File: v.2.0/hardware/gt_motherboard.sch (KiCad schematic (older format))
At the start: 68 parts, among them Q1 MMBT2222, Q2 IRLML6302, Q3 MMBT2222, SW1 SWITCH, U1 L6470

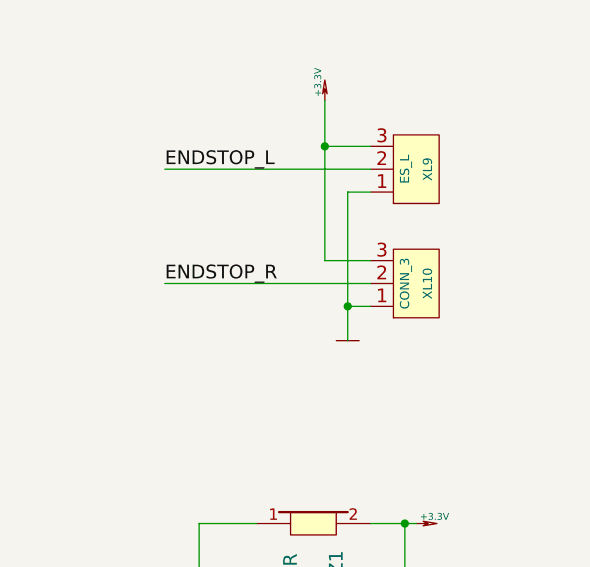
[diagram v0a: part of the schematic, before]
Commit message: + Assign all components.
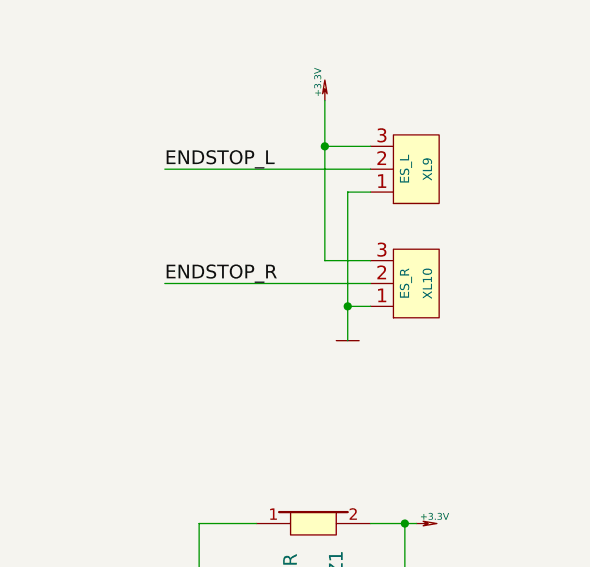
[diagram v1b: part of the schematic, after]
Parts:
- C16: footprint (none) -> Capacitors:CAP_08xxR
- C24: footprint (none) -> Capacitors:CAP_06xxR
- D1, D3, D4: footprint Diodes:SOD80C -> LEDs:LED_0603
- D5, D6: footprint Diodes:SOD323 -> Diodes:SOD80C
- U1: footprint (none) -> Installation:HTSSOP28
- XL10: value CONN_3 -> ES_R
- XL4: footprint Installation:2xBAT_AA_SOLDER -> Socket_Strips:Socket_Strip_Straight_1x02_Pitch2.54mm
- XL6, XL7: footprint (none) -> Socket_Strips:Socket_Strip_Straight_1x02_Pitch2.54mm
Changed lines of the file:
@@
 F 0 "U1" H 14050 3700 60  0000 C CNN
 F 1 "L6470" H 14100 3850 60  0000 C CNN
-F 2 "" H 8600 4700 60  0001 C CNN
+F 2 "Installation:HTSSOP28" H 8600 4700 60  0001 C CNN
 F 3 "" H 8600 4700 60  0000 C CNN
 	1    13100 3050
@@
 F 0 "XL6" V 14700 3050 40  0000 C CNN
 F 1 "CONN_2" V 14800 3050 40  0000 C CNN
-F 2 "" H 14750 3050 60  0001 C CNN
+F 2 "Socket_Strips:Socket_Strip_Straight_1x02_Pitch2.54mm" H 14750 3050 60  0001 C CNN
 F 3 "" H 14750 3050 60  0000 C CNN
 	1    14750 3050
@@
 F 0 "XL7" V 14700 3550 40  0000 C CNN
 F 1 "CONN_2" V 14800 3550 40  0000 C CNN
-F 2 "" H 14750 3550 60  0001 C CNN
+F 2 "Socket_Strips:Socket_Strip_Straight_1x02_Pitch2.54mm" H 14750 3550 60  0001 C CNN
 F 3 "" H 14750 3550 60  0000 C CNN
 	1    14750 3550
@@
 F 0 "D5" H 12900 1250 40  0000 C CNN
 F 1 "1N4148" H 12900 1050 40  0000 C CNN
-F 2 "Diodes:SOD323" H 12900 1150 60  0001 C CNN
+F 2 "Diodes:SOD80C" H 12900 1150 60  0001 C CNN
 F 3 "" H 12900 1150 60  0000 C CNN
 	1    12900 1150
@@
 F 0 "D6" H 13550 1250 40  0000 C CNN
 F 1 "1N4148" H 13550 1050 40  0000 C CNN
-F 2 "Diodes:SOD323" H 13550 1150 60  0001 C CNN
+F 2 "Diodes:SOD80C" H 13550 1150 60  0001 C CNN
 F 3 "" H 13550 1150 60  0000 C CNN
 	1    13550 1150
@@
 F 0 "C24" H 15550 2050 50  0000 L CNN
 F 1 "100u/50V" V 15350 1800 50  0000 L CNN
-F 2 "" H 15500 1950 60  0001 C CNN
+F 2 "Capacitors:CAP_06xxR" H 15500 1950 60  0001 C CNN
 F 3 "" H 15500 1950 60  0000 C CNN
 	1    15500 1950
@@
 F 0 "C16" H 12100 1800 50  0000 L CNN
 F 1 "4u7/63V" V 12350 1750 50  0000 L CNN
-F 2 "" H 12200 1900 60  0001 C CNN
+F 2 "Capacitors:CAP_08xxR" H 12200 1900 60  0001 C CNN
 F 3 "" H 12200 1900 60  0000 C CNN
 	1    12200 1900
@@
 F 0 "D3" H 10850 1990 50  0000 C CNN
 F 1 "LED" H 10670 1990 50  0000 C CNN
-F 2 "Diodes:SOD80C" H 10750 1850 60  0001 C CNN
+F 2 "LEDs:LED_0603" H 10750 1850 60  0001 C CNN
 F 3 "" H 10750 1850 60  0000 C CNN
 	1    10750 1850
@@
 F 0 "D4" H 11150 1990 50  0000 C CNN
 F 1 "LED" H 10970 1990 50  0000 C CNN
-F 2 "Diodes:SOD80C" H 11050 1850 60  0001 C CNN
+F 2 "LEDs:LED_0603" H 11050 1850 60  0001 C CNN
 F 3 "" H 11050 1850 60  0000 C CNN
 	1    11050 1850
@@
 F 0 "XL4" V 1300 9100 40  0000 C CNN
 F 1 "CONN_2" V 1400 9100 40  0000 C CNN
-F 2 "Installation:2xBAT_AA_SOLDER" H 1350 9100 60  0001 C CNN
+F 2 "Socket_Strips:Socket_Strip_Straight_1x02_Pitch2.54mm" H 1350 9100 60  0001 C CNN
 F 3 "" H 1350 9100 60  0000 C CNN
 	1    1350 9100
@@
 F 0 "D1" H 3050 6590 50  0000 C CNN
 F 1 "LED" H 2870 6590 50  0000 C CNN
-F 2 "Diodes:SOD80C" H 2950 6450 60  0001 C CNN
+F 2 "LEDs:LED_0603" H 2950 6450 60  0001 C CNN
 F 3 "" H 2950 6450 60  0000 C CNN
 	1    2950 6450
@@
 P 15200 6200
 F 0 "XL10" V 15150 6200 40  0000 C CNN
-F 1 "CONN_3" V 15250 6200 40  0000 C CNN
+F 1 "ES_R" V 15250 6200 40  0000 C CNN
 F 2 "Socket_Strips:Socket_Strip_Straight_1x03_Pitch2.54mm" H 15200 6200 60  0001 C CNN
 F 3 "" H 15200 6200 60  0000 C CNN
